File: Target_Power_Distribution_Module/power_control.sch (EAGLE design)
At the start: 7 parts, among them Q1 NFET, Q2 PFET

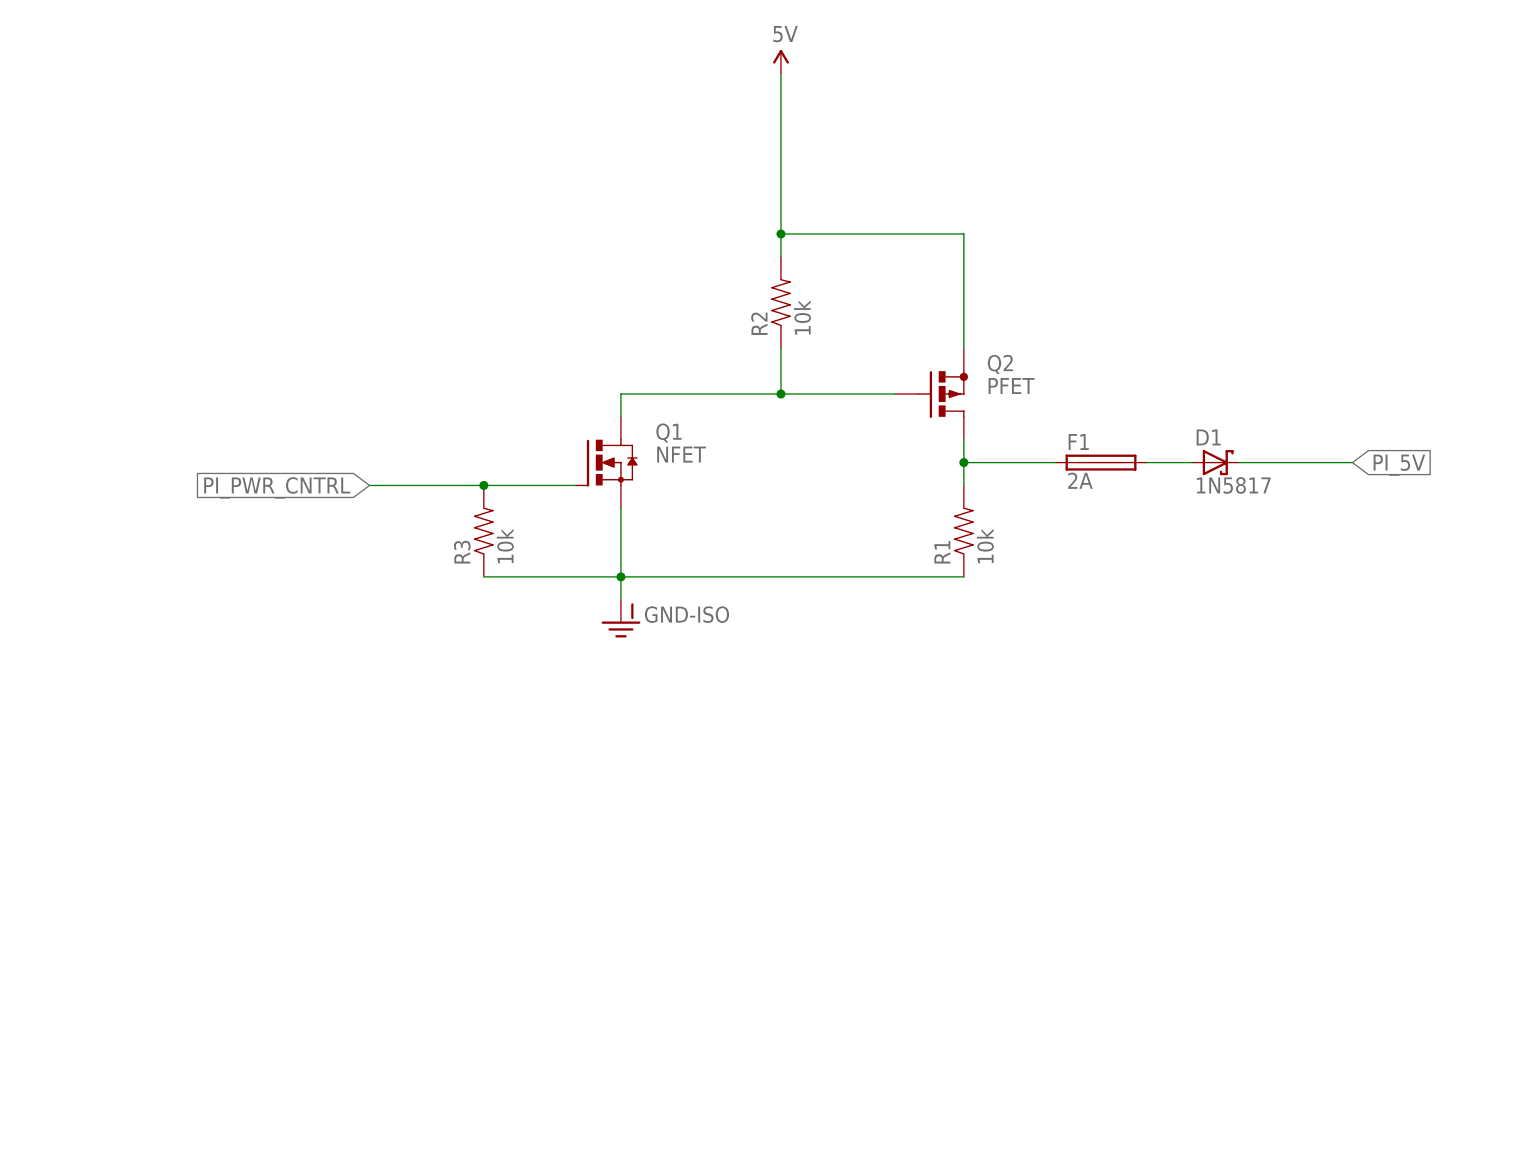
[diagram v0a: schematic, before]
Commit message: Added power control
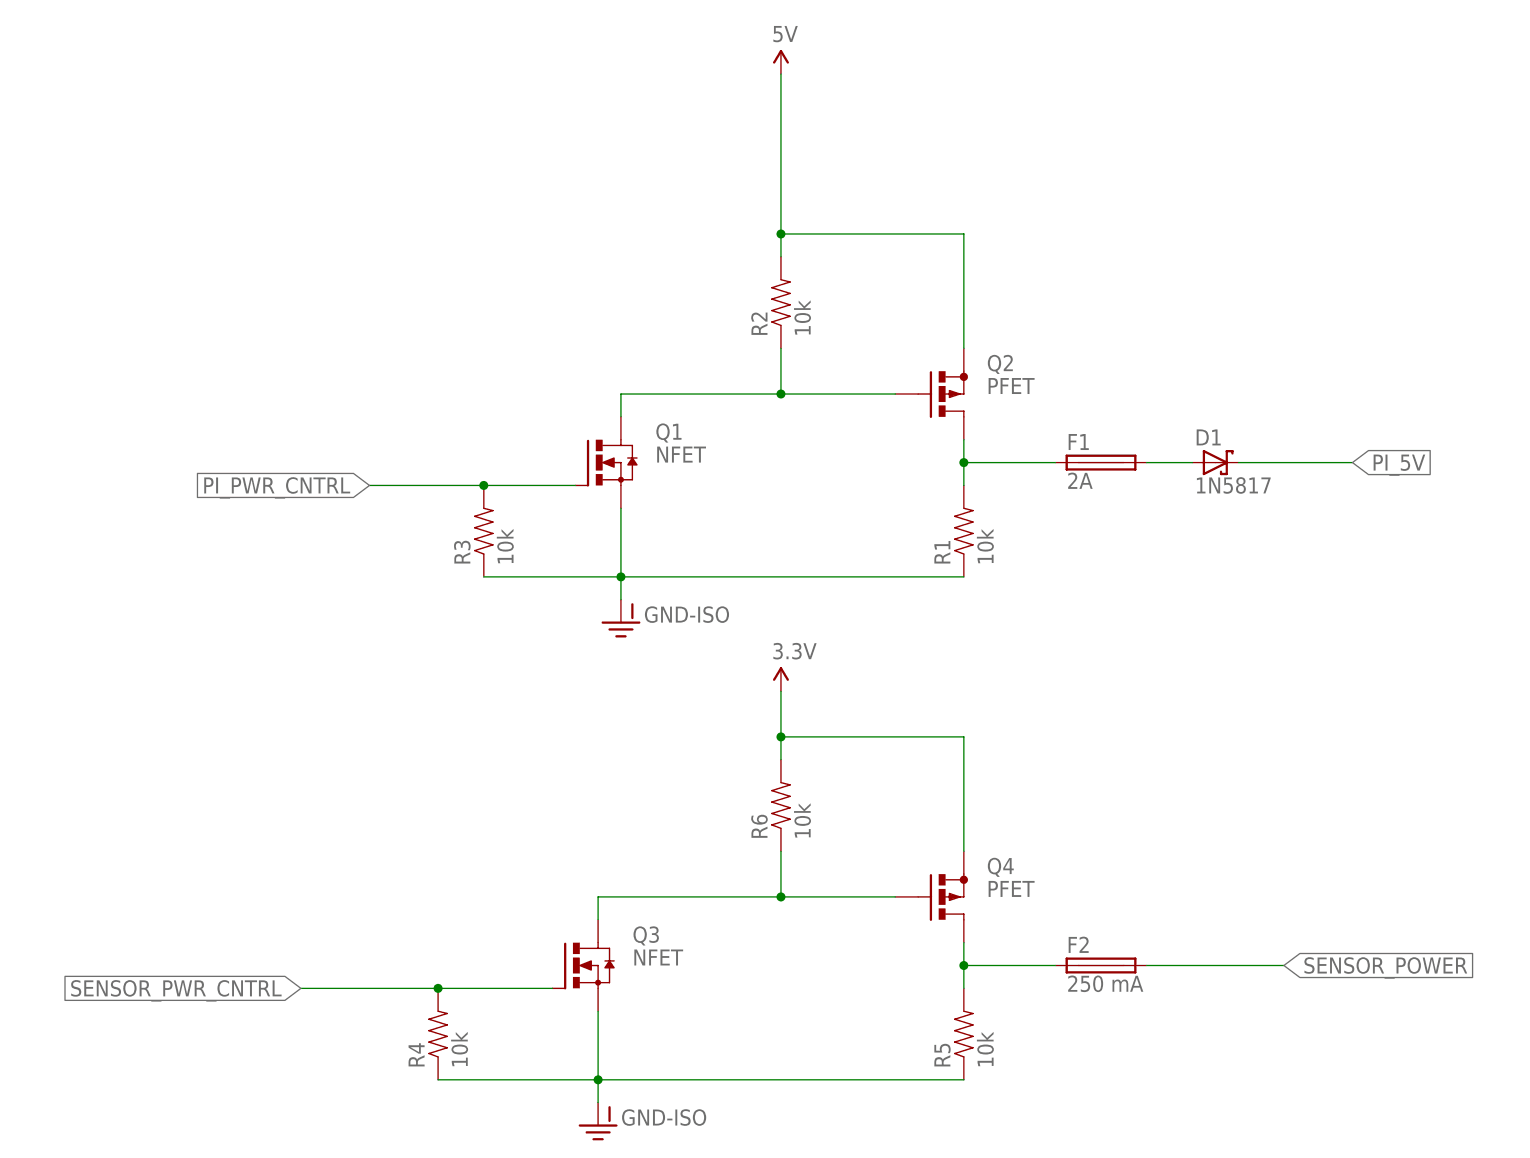
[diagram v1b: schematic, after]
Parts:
- added F2: 250 mA, fuse:FUSEPICOFUSE
- added Q3: NFET, transistor-power:IRF3704
- added Q4: PFET, adafruit:PFETBS250
- added R4, R5, R6: 10k, SparkFun-Resistors:RESISTOR1206
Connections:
- net VCC renamed 5V
- new net 3.3V: Q4.S, R6.2
- new net N$1: Q3.D, Q4.G, R6.1
- new net N$6: F2.1, Q4.D, R5.2
- new net SENSOR_POWER: F2.2
- new net SENSOR_PWR_CNTRL: Q3.G, R4.2
- net GND-ISO: now also Q3.S, R4.1, R5.1
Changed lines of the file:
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@@
 <part name="D1" library="adafruit" deviceset="SCHOTTKY-DIODE" device="CB429-15" value="1N5817"/>
 <part name="F1" library="fuse" deviceset="FUSE" device="PICOFUSE" value="2A"/>
+<part name="Q3" library="transistor-power" deviceset="IRF3704" device="" value="NFET"/>
+<part name="Q4" library="adafruit" deviceset="PFET" device="BS250" value="PFET"/>
+<part name="F2" library="fuse" deviceset="FUSE" device="PICOFUSE" value="250 mA"/>
+<part name="R4" library="SparkFun-Resistors" deviceset="RESISTOR" device="1206" value="10k"/>
+<part name="R5" library="SparkFun-Resistors" deviceset="RESISTOR" device="1206" value="10k"/>
+<part name="R6" library="SparkFun-Resistors" deviceset="RESISTOR" device="1206" value="10k"/>
+<part name="3.3V" library="SparkFun-Aesthetics" deviceset="VCC" device="" value="3.3V"/>
+<part name="GND-ISO2" library="SparkFun-Aesthetics" deviceset="GND-ISO" device=""/>
 </parts>
 <sheets>
@@
 <instance part="D1" gate="G$1" x="96.52" y="48.26"/>
 <instance part="F1" gate="G$1" x="83.82" y="48.26"/>
+<instance part="Q3" gate="G$1" x="25.4" y="-7.62"/>
+<instance part="Q4" gate="1" x="66.04" y="0"/>
+<instance part="F2" gate="G$1" x="83.82" y="-7.62"/>
+<instance part="R4" gate="G$1" x="10.16" y="-15.24" rot="R90"/>
+<instance part="R5" gate="G$1" x="68.58" y="-15.24" rot="R90"/>
+<instance part="R6" gate="G$1" x="48.26" y="10.16" rot="R90"/>
+<instance part="3.3V" gate="G$1" x="48.26" y="22.86"/>
+<instance part="GND-ISO2" gate="G$1" x="27.94" y="-25.4"/>
 </instances>
 <busses>
@@
 <wire x1="30.48" y1="35.56" x2="68.58" y2="35.56" width="0.1524" layer="91"/>
 </segment>
-</net>
-<net name="VCC" class="0">
 <segment>
-<pinref part="Q2" gate="1" pin="S"/>
-<wire x1="68.58" y1="60.96" x2="68.58" y2="73.66" width="0.1524" layer="91"/>
-<pinref part="SUPPLY1" gate="G$1" pin="VCC"/>
-<wire x1="68.58" y1="73.66" x2="48.26" y2="73.66" width="0.1524" layer="91"/>
-<wire x1="48.26" y1="73.66" x2="48.26" y2="91.44" width="0.1524" layer="91"/>
-<pinref part="R2" gate="G$1" pin="2"/>
-<wire x1="48.26" y1="73.66" x2="48.26" y2="71.12" width="0.1524" layer="91"/>
-<junction x="48.26" y="73.66"/>
+<pinref part="R4" gate="G$1" pin="1"/>
+<pinref part="GND-ISO2" gate="G$1" pin="GND-ISO"/>
+<wire x1="10.16" y1="-20.32" x2="27.94" y2="-20.32" width="0.1524" layer="91"/>
+<wire x1="27.94" y1="-20.32" x2="27.94" y2="-22.86" width="0.1524" layer="91"/>
+<pinref part="R5" gate="G$1" pin="1"/>
+<wire x1="27.94" y1="-20.32" x2="68.58" y2="-20.32" width="0.1524" layer="91"/>
+<junction x="27.94" y="-20.32"/>
+<pinref part="Q3" gate="G$1" pin="S"/>
+<wire x1="27.94" y1="-12.7" x2="27.94" y2="-20.32" width="0.1524" layer="91"/>
 </segment>
 </net>
@@
 </segment>
 </net>
+<net name="N$1" class="0">
+<segment>
+<pinref part="Q4" gate="1" pin="G"/>
+<pinref part="R6" gate="G$1" pin="1"/>
+<wire x1="60.96" y1="0" x2="48.26" y2="0" width="0.1524" layer="91"/>
+<wire x1="48.26" y1="0" x2="48.26" y2="5.08" width="0.1524" layer="91"/>
+<pinref part="Q3" gate="G$1" pin="D"/>
+<wire x1="27.94" y1="-2.54" x2="27.94" y2="0" width="0.1524" layer="91"/>
+<wire x1="27.94" y1="0" x2="48.26" y2="0" width="0.1524" layer="91"/>
+<junction x="48.26" y="0"/>
+</segment>
+</net>
+<net name="3.3V" class="0">
+<segment>
+<pinref part="Q4" gate="1" pin="S"/>
+<wire x1="68.58" y1="5.08" x2="68.58" y2="17.78" width="0.1524" layer="91"/>
+<wire x1="68.58" y1="17.78" x2="48.26" y2="17.78" width="0.1524" layer="91"/>
+<pinref part="R6" gate="G$1" pin="2"/>
+<wire x1="48.26" y1="17.78" x2="48.26" y2="15.24" width="0.1524" layer="91"/>
+<pinref part="3.3V" gate="G$1" pin="VCC"/>
+<wire x1="48.26" y1="17.78" x2="48.26" y2="22.86" width="0.1524" layer="91"/>
+<junction x="48.26" y="17.78"/>
+</segment>
+</net>
+<net name="5V" class="0">
+<segment>
+<pinref part="Q2" gate="1" pin="S"/>
+<wire x1="68.58" y1="60.96" x2="68.58" y2="73.66" width="0.1524" layer="91"/>
+<pinref part="SUPPLY1" gate="G$1" pin="VCC"/>
+<wire x1="68.58" y1="73.66" x2="48.26" y2="73.66" width="0.1524" layer="91"/>
+<wire x1="48.26" y1="73.66" x2="48.26" y2="91.44" width="0.1524" layer="91"/>
+<pinref part="R2" gate="G$1" pin="2"/>
+<wire x1="48.26" y1="73.66" x2="48.26" y2="71.12" width="0.1524" layer="91"/>
+<junction x="48.26" y="73.66"/>
+</segment>
+</net>
+<net name="SENSOR_PWR_CNTRL" class="0">
+<segment>
+<pinref part="R4" gate="G$1" pin="2"/>
+<pinref part="Q3" gate="G$1" pin="G"/>
+<wire x1="10.16" y1="-10.16" x2="22.86" y2="-10.16" width="0.1524" layer="91"/>
+<wire x1="10.16" y1="-10.16" x2="-5.08" y2="-10.16" width="0.1524" layer="91"/>
+<junction x="10.16" y="-10.16"/>
+<label x="-5.08" y="-10.16" size="1.778" layer="95" rot="R180" xref="yes"/>
+</segment>
+</net>
+<net name="N$6" class="0">
+<segment>
+<pinref part="Q4" gate="1" pin="D"/>
+<pinref part="R5" gate="G$1" pin="2"/>
+<wire x1="68.58" y1="-5.08" x2="68.58" y2="-7.62" width="0.1524" layer="91"/>
+<pinref part="F2" gate="G$1" pin="1"/>
+<wire x1="68.58" y1="-7.62" x2="68.58" y2="-10.16" width="0.1524" layer="91"/>
+<wire x1="68.58" y1="-7.62" x2="78.74" y2="-7.62" width="0.1524" layer="91"/>
+<junction x="68.58" y="-7.62"/>
+</segment>
+</net>
+<net name="SENSOR_POWER" class="0">
+<segment>
+<pinref part="F2" gate="G$1" pin="2"/>
+<wire x1="88.9" y1="-7.62" x2="104.14" y2="-7.62" width="0.1524" layer="91"/>
+<label x="104.14" y="-7.62" size="1.778" layer="95" xref="yes"/>
+</segment>
+</net>
